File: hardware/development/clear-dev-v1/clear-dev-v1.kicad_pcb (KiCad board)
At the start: 2 copper layers, 76.2 x 73.8 mm, 77 parts, among them J1 USB_B_Micro, J10 Conn_01x28_Pin, J11 Conn_01x28_Pin, J2 Conn_01x02_Pin, J3 Conn_01x02_Pin, J4 Conn_01x03_Pin, J5 Conn_01x02_Pin, J6 Conn_01x02_Pin, J7 Conn_01x06_Pin, J8 Conn_01x02_Pin, J9 Conn_01x02_Pin, SW1 SW_Push - SKQGADE010, T1 Logo, T2 Logo, U1 FT232H, U10 DS1086LU, U2 SN74LVC1G125DCKR, U3 SN74LVC1G125DCKR, U5 TAR5SxxU, U6 TAR5SxxU, U7 W25Q32FVSS, U8 M.2-CONNECTOR-E, U9 TMUX4053-BQB, X1 DSC6001_10MHZ, Y1 12MHz

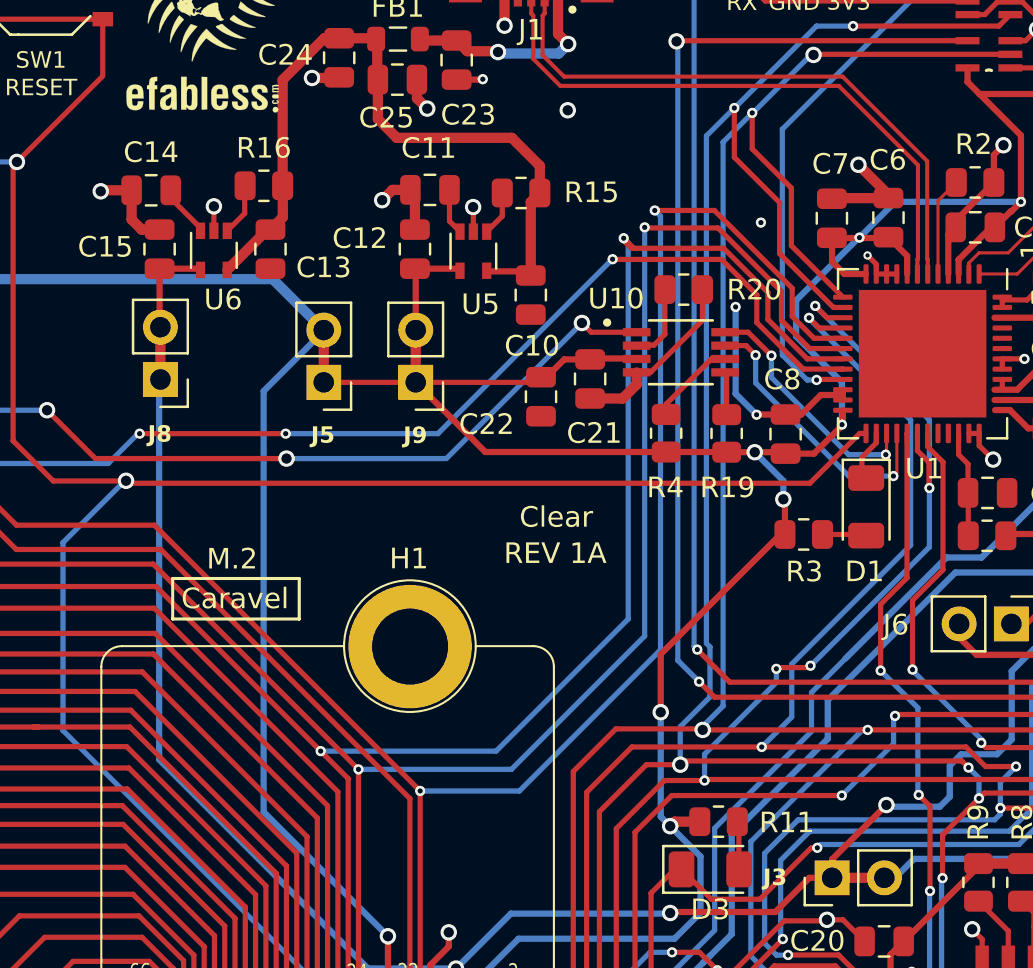
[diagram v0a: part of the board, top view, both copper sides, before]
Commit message: ~ update clear PCB with test pads for clock generator dither enable and power-down mode enable to allow enabling them if needed
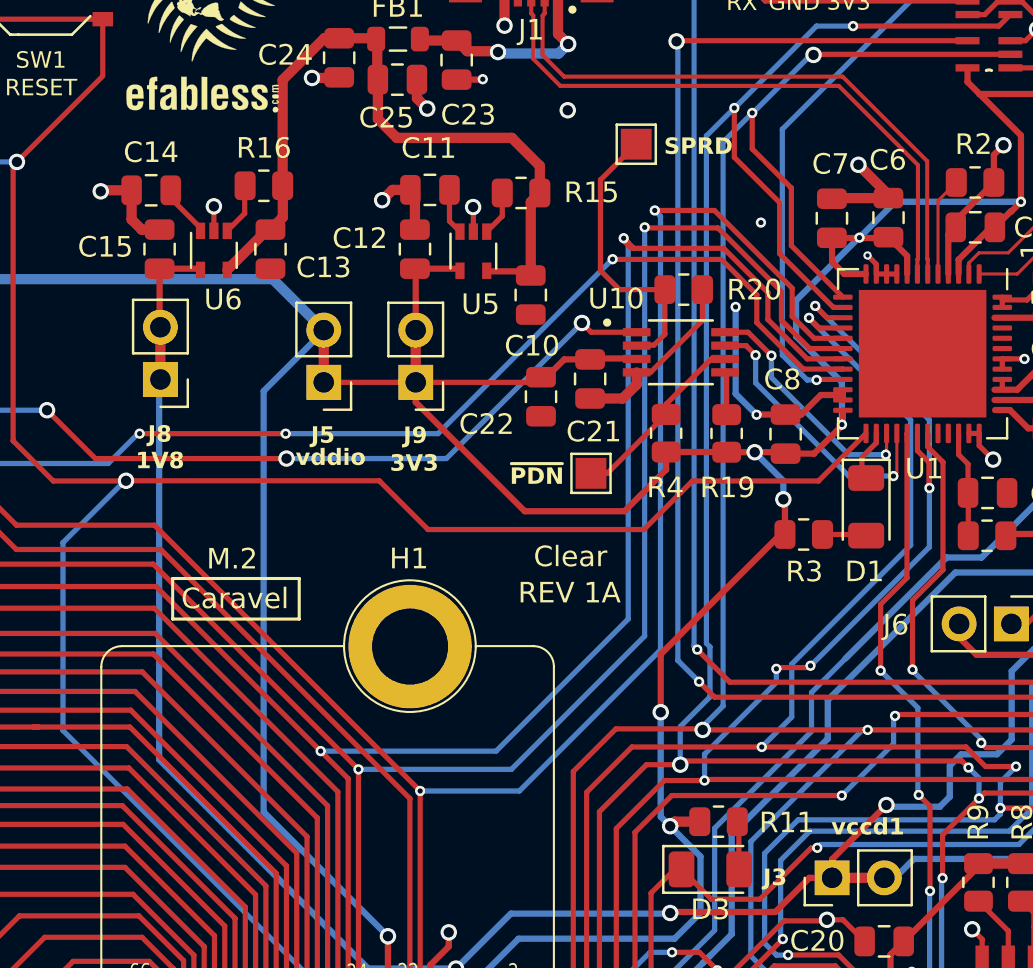
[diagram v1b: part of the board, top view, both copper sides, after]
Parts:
- added TP3: TestPoint, TestPoint:TestPoint_Pad_1.5x1.5mm, F.Cu at (137.1, 129.3)
- added TP4: TestPoint, TestPoint:TestPoint_Pad_1.5x1.5mm, F.Cu at (134.9, 145.3)
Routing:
- net Net-(U10-SPRD): track 3.79 -> 14.2 mm
- net Net-(U10-~{PDN}): track 4.28 -> 9.12 mm
- net +3V3: track 392.8 -> 396.3 mm
- net /~{RST}: track 127.8 -> 129.7 mm
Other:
- board text added: "SPRD"
- board text added: "~{PDN}"

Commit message: ~ update clear dev pcb
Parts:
- removed TP4: TestPoint, TestPoint:TestPoint_Pad_1.5x1.5mm
- added J12: Conn_01x02_Pin, Connector_PinHeader_2.54mm:PinHeader_1x02_P2.54mm_Vertical, F.Cu at (118.0, 141.9)
- added U4: SN74LVC1G125DCKR, strive_foot_prints:SOT65P210X110-5N, F.Cu at (143.2, 153.1)
- TP3: footprint TestPoint:TestPoint_Pad_1.5x1.5mm -> TestPoint:TestPoint_THTPad_2.0x2.0mm_Drill1.0mm
- moved TP3 0.93 mm to (136.2, 129.2)
- turned R18 to 180 degrees
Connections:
- net /~{RST} renamed /ACBUS1
- net /~{UART_EN} renamed /ACBUS0
- net Net-(D1-K) renamed /ACBUS2
- net Net-(J6-Pin_1) renamed /OSC_EN
- net Net-(U10-SPRD) renamed /SPRD
- net Net-(U10-~{PDN}) renamed /~{PDN}
- net gpio renamed /gpio
- J7 pad 2: /ACBUS6 -> /Caravel_D1
- R18 pad 1: GND -> +3V3
- R8 pad 1: /ACBUS6 -> /Caravel_D1
- U7 pad 2: /ACBUS6 -> /Caravel_D1
- U8 pad 19: /ACBUS6 -> /Caravel_D1
- U9 pad 1: /USB_CS1 -> /Caravel_CSB
- U9 pad 12: /Caravel_D0 -> /USB_SO_RXD
- U9 pad 13: /USB_SO_RXD -> /Caravel_D0
- U9 pad 2: /Caravel_CSB -> /USB_CS1
- U9 pad 3: /USB_SCK_TXD -> /Caravel_SCK
- U9 pad 5: /Caravel_SCK -> /USB_SCK_TXD
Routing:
- net /Caravel_D1: track 0.00 -> 91.4 mm, vias 0 -> 9
- net /ACBUS6: track 178.2 -> 103.0 mm, vias 13 -> 4
- net /~{PDN}: track 9.12 -> 28.2 mm, vias 0 -> 1
- net +3V3: track 396.3 -> 414.2 mm, vias 17 -> 19
- net /ACBUS5: track 38.5 -> 45.4 mm
- net GND: track 116.9 -> 115.4 mm, vias 35 -> 36
- net /~{MEM_CS}: track 38.6 -> 40.1 mm
- net /USB_SCK_TXD: track 149.8 -> 151.3 mm
- net /mprj_io[5]_ser_rx: track 147.5 -> 148.9 mm
- net /ACBUS0: track 45.1 -> 43.9 mm
- net /ADBUS5: track 112.0 -> 113.0 mm
- net /mprj_io[6]_ser_tx: track 151.0 -> 151.9 mm
- net /~{MEM_WP}: track 30.7 -> 31.6 mm
- net /Caravel_CSB: track 28.8 -> 29.6 mm
- net /USB_SO_RXD: track 145.5 -> 146.2 mm
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
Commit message: ~ update clear dev pcb
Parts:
- moved R17 0.20 mm to (146.2, 174.5)
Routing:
- net /USB_SCK_TXD: track 151.3 -> 151.9 mm

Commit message: ~ update clear dev pcb
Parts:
- moved R11 39.5 mm to (162.2, 128.8), turned to -90 degrees
- moved D3 37.4 mm to (162.8, 134.4), turned to 90 degrees
- moved U4 2.33 mm to (145.6, 153.0)
- moved T1 0.69 mm to (116.5, 122.5)
- moved T2 0.43 mm to (116.3, 127.2)
- moved Y1 0.12 mm to (158.4, 130.1)
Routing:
- net GND: track 115.4 -> 97.4 mm, vias 36 -> 35
- net /gpio: track 83.2 -> 92.6 mm, vias 4 -> 5
- net +3V3: track 414.2 -> 416.7 mm, vias 19 -> 18
- net /ACBUS5: track 45.4 -> 42.9 mm
- net /USB_CS1: track 123.2 -> 122.0 mm
- net /ACBUS1: track 129.7 -> 128.6 mm
- net Net-(D3-A): track 2.52 -> 3.67 mm
- net /ADBUS7: track 97.6 -> 98.7 mm
- net /Caravel_D1: track 91.4 -> 92.0 mm, vias 9 -> 8
- net /~{MEM_CS}: track 40.0 -> 39.5 mm, vias 4 -> 2
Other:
- board text added: "CLK GEN"
- board text added: "OSC EN"

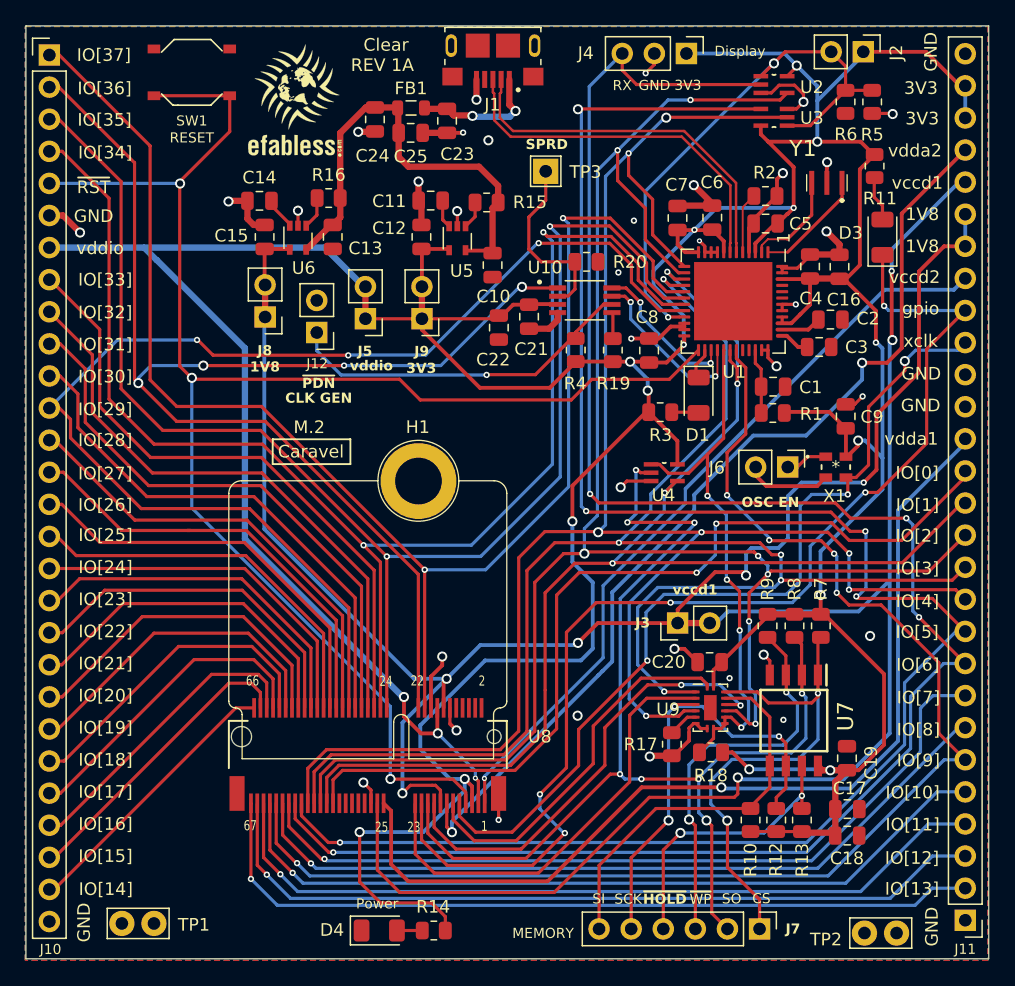
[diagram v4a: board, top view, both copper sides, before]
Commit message: update clear dev board to REV 1B
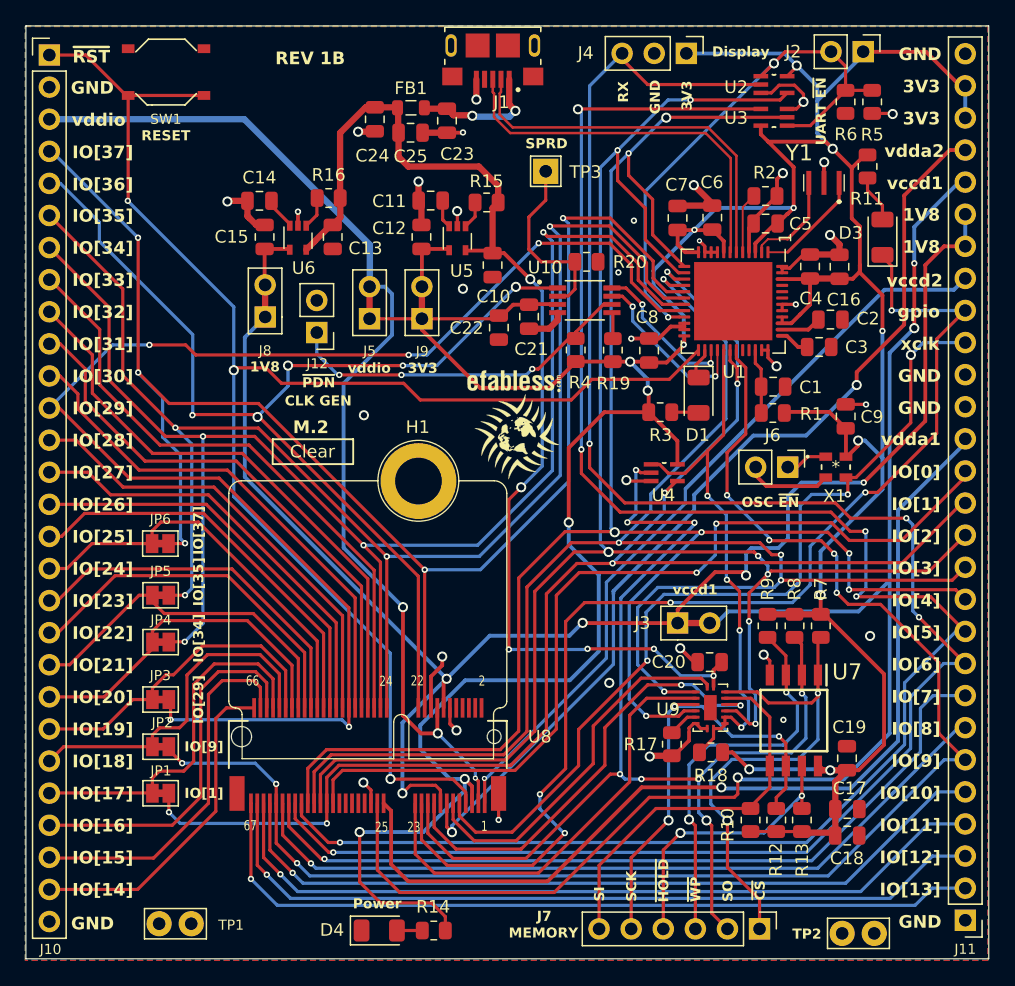
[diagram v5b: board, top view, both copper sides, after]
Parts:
- added JP1: SolderJumper_2_Bridged, Jumper:SolderJumper-2_P1.3mm_Bridged_Pad1.0x1.5mm, F.Cu at (105.7, 178.4)
- added JP2: SolderJumper_2_Bridged, Jumper:SolderJumper-2_P1.3mm_Bridged_Pad1.0x1.5mm, F.Cu at (105.7, 174.7)
- added JP3: SolderJumper_2_Bridged, Jumper:SolderJumper-2_P1.3mm_Bridged_Pad1.0x1.5mm, F.Cu at (105.7, 171.0)
- added JP4: SolderJumper_2_Bridged, Jumper:SolderJumper-2_P1.3mm_Bridged_Pad1.0x1.5mm, F.Cu at (105.7, 166.4)
- added JP5: SolderJumper_2_Bridged, Jumper:SolderJumper-2_P1.3mm_Bridged_Pad1.0x1.5mm, F.Cu at (105.7, 162.7)
- added JP6: SolderJumper_2_Bridged, Jumper:SolderJumper-2_P1.3mm_Bridged_Pad1.0x1.5mm, F.Cu at (105.7, 158.6)
- J3, J5, J8, J9: footprint Connector_PinHeader_2.54mm:PinHeader_1x02_P2.54mm_Vertical -> Caravel_Board:Shorted_PinHeader_1x02_P2.54mm_Vertical
- moved T1 32.7 mm to (133.9, 150.2)
- moved T2 25.5 mm to (133.6, 145.8)
- moved TP1 2.95 mm to (108.1, 188.7)
- moved SW1 2.04 mm to (106.1, 121.3)
- moved TP2 1.77 mm to (162.2, 189.5)
- moved R11 0.56 mm to (161.6, 128.8)
- moved J5 0.33 mm to (122.2, 140.9)
- moved Y1 0.23 mm to (158.2, 130.1)
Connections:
- C20 pad 2: +3V3 -> +5V
- J10 pad 1: /ADBUS4 -> /ACBUS1
- J10 pad 2: /CLK_GEN -> GND
- J10 pad 3: /ADBUS5 -> +3V3
- J10 pad 4: /ADBUS6 -> /ADBUS4
- J10 pad 5: /ACBUS1 -> /CLK_GEN
- J10 pad 6: GND -> /ADBUS5
- J10 pad 7: +3V3 -> /ADBUS6
- U9 pad 16: +3V3 -> +5V
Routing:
- net +5V: track 36.3 -> 90.3 mm, vias 0 -> 6
- net /ADBUS7: track 98.7 -> 115.0 mm, vias 3 -> 5
- net /CLK_GEN: track 102.4 -> 86.2 mm, vias 4 -> 5
- net /ACBUS6: track 102.5 -> 118.4 mm, vias 4 -> 6
- net /ACBUS7: track 107.5 -> 118.9 mm, vias 5 -> 7
- net /ADBUS6: track 111.1 -> 120.5 mm, vias 2 -> 4
- net /ADBUS4: track 116.7 -> 125.3 mm, vias 2 -> 5
- net /ADBUS5: track 113.0 -> 119.4 mm, vias 2 -> 4
- net GND: track 97.4 -> 91.3 mm, vias 35 -> 33
- net /mprj_io[15]: track 23.9 -> 29.4 mm
- net /ACBUS1: track 128.6 -> 123.3 mm
- net /mprj_io[16]: track 24.4 -> 29.6 mm
- net /mprj_io[14]: track 22.2 -> 26.5 mm
- net /mprj_io[24]: track 28.9 -> 32.5 mm
- net +3V3: track 416.7 -> 413.5 mm
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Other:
- board text added: "OSC ~{EN}"
- board text added: "REV 1B"
- board text added: "UART ~{EN}"
- board text added: "~{CS}"
- board text removed: "CS"
- board text removed: "Caravel"
- board text removed: "OSC EN"
- board text removed: "REV 1A"

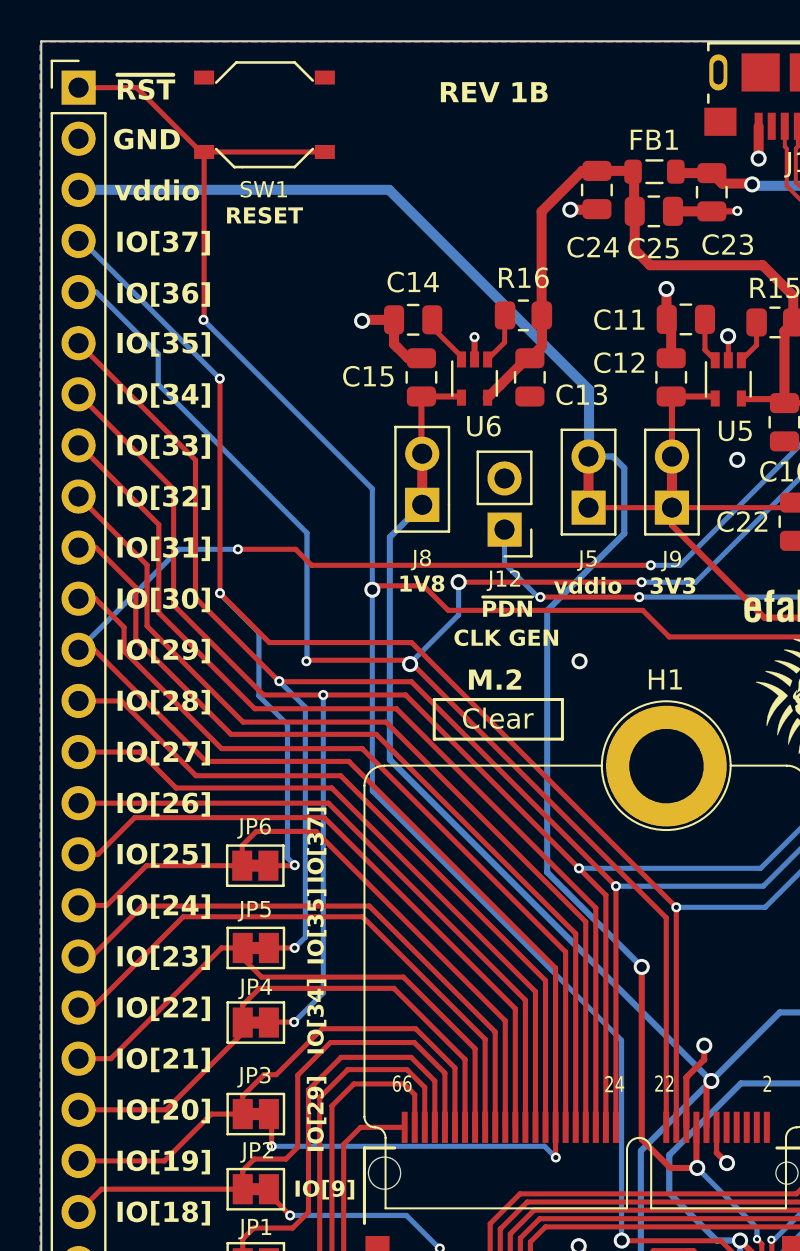
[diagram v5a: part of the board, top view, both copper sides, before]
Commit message: update clear dev board to REV 1B after layout review
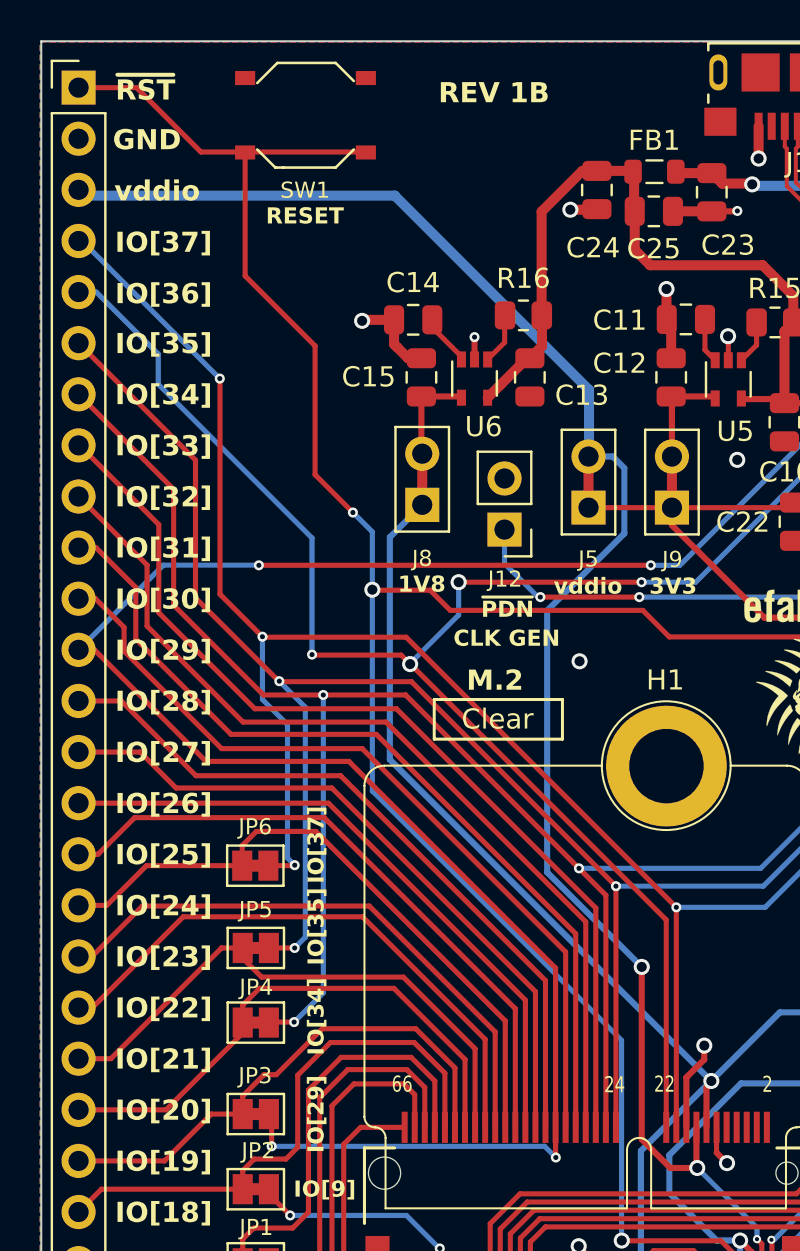
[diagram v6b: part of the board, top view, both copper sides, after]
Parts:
- moved SW1 2.04 mm to (108.2, 121.4)
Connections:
- net /OSC_EN renamed /OSC_~{EN}
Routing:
- net /ADBUS4: track 125.3 -> 122.3 mm
- net /ACBUS1: track 123.3 -> 124.3 mm
- net /ADBUS7: track 115.0 -> 114.3 mm

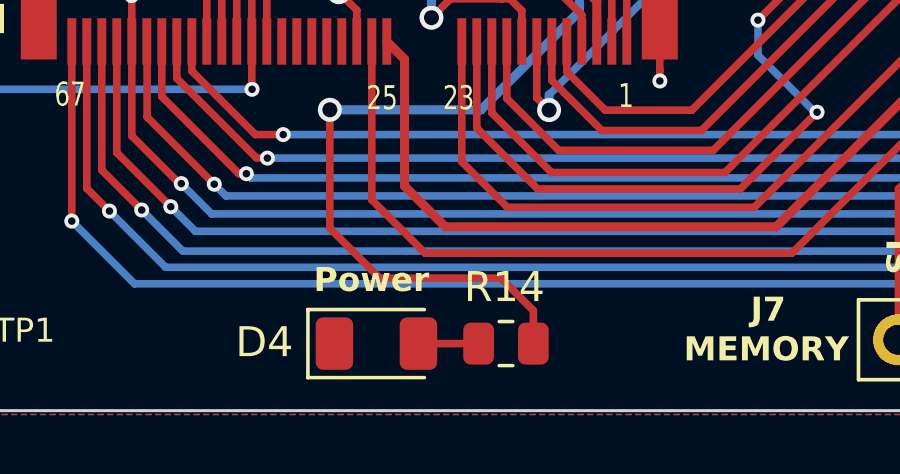
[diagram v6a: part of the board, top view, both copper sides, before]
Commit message: update clear board REV 1B
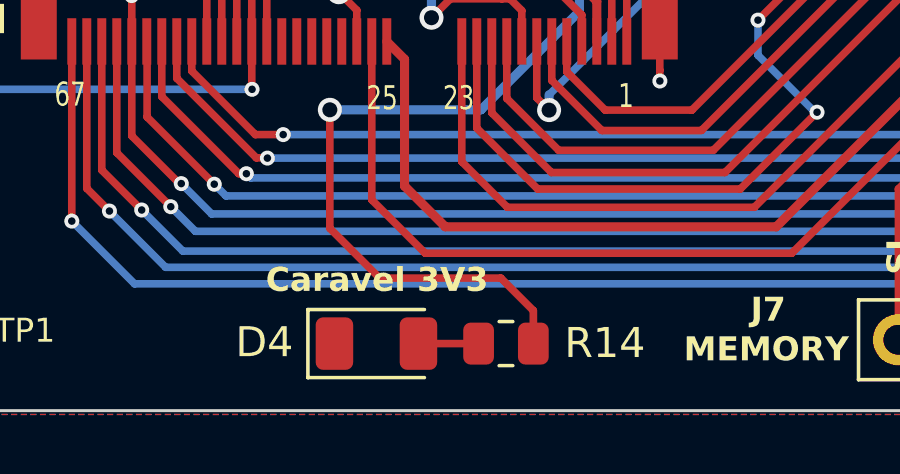
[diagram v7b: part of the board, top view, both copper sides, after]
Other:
- board text added: "Caravel 3V3"
- board text removed: "Power"
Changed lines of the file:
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@@
     (property "ki_keywords" "R res resistor")
     (attr smd)
-    (fp_text reference "R14" (at 0.0508 1.8796) (layer "F.SilkS")
+    (fp_text reference "R14" (at -3.2964 0.0174) (layer "F.SilkS")
         (effects (font (size 1 1) (thickness 0.15)))
     )
@@
     (effects (font (size 1 1) (thickness 0.2) bold))
   )
-  (gr_text "Power" (at 122.8272 187.15) (layer "F.SilkS" knockout)
+  (gr_text "Caravel 3V3" (at 123.0122 187.1472) (layer "F.SilkS" knockout)
     (effects (font (size 0.8 0.8) (thickness 0.16) bold))
   )
